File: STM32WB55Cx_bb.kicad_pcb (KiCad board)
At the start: 2 copper layers, 17.8 x 38.1 mm, 32 parts, among them J1 Prog, J2 USB, J3 GPIO1, J4 GPIO2, U1 STM32WB55Cx, U2 LDFM, Y1 LSE, Y2 32MHz

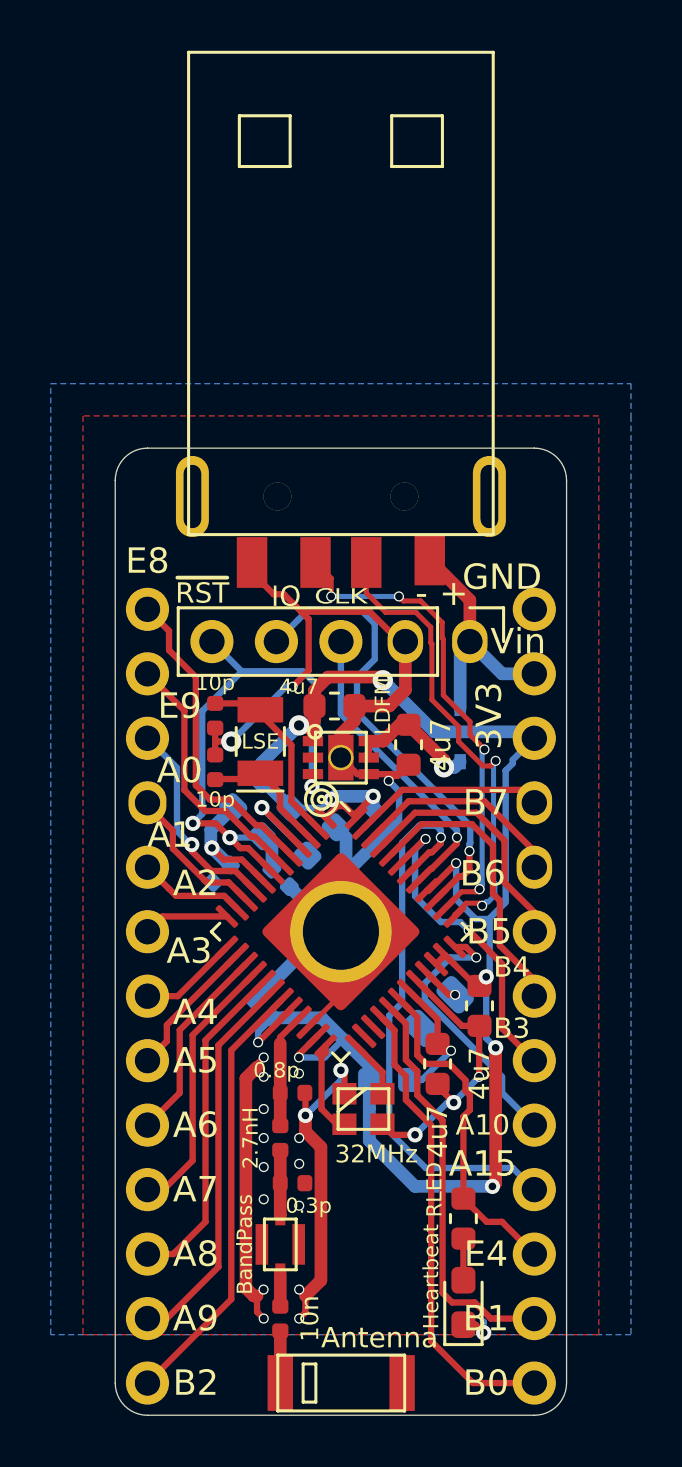
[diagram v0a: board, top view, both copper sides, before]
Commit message: Minor silkscreen changes; make pin numbers more legible, and add an OSHW logo on the bottom.
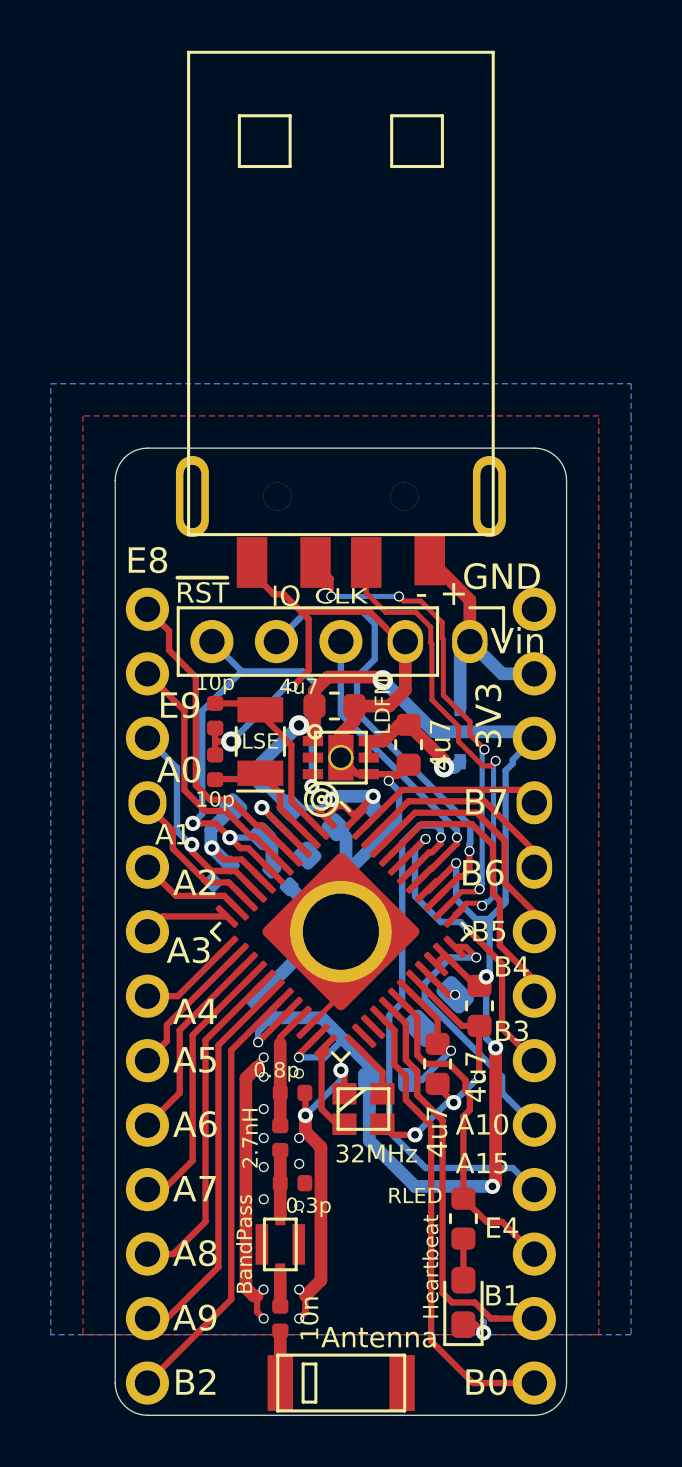
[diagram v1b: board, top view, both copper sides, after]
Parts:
- added G***: LOGO, STM32WB55Cx_bb:oshw_logo, B.Cu at (210.8, 108.8)
